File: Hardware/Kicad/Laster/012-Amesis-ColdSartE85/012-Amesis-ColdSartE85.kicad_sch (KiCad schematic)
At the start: 1 part

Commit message: kicad en cour
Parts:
- added G2/G62_InPut_IAT, G2/G62_OutPut_IAT: Conn_01x04_Male, symbol Connector:Conn_01x04_Male
- added IAT_Interne: R_Potentiometer, symbol Device:R_Potentiometer
- added Jumpers_Option: Conn_01x03_Male, symbol Connector:Conn_01x03_Male
- added X9C103S: Conn_01x08_Male, symbol Connector:Conn_01x08_Male
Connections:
- net at A?.26 (A7): now also IAT_Interne.2
- net at A?.27 (+5V): now also IAT_Interne.3
- net GND: now reaches A?.29 (GND)
- net GND: now also A?.4 (GND), IAT_Interne.1
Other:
- title: (none) -> 012-Amesis-ColdStartE85
- moved on the sheet: A?
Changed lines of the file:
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@@
   (paper "A4")
   (title_block
-    (date "2022-09-11")
-    (rev "v0.01")
-  )
-  (symbol (lib_id "MCU_Module:Arduino_Nano_v3.x") (at 129.794 87.122 0) (unit 1)
-    (in_bom yes) (on_board yes) (fields_autoplaced)
-    (property "Reference" "A?" (id 0) (at 134.3534 112.1315 0)
+    (title "012-Amesis-ColdStartE85")
+    (date "2022-09-15")
+    (rev "v0.01_Golf 1.6L 16v ")
+  )
+  (junction (at 133.858 97.282) (diameter 0) (color 0 0 0 0)
+  )
+  (junction (at 136.398 97.282) (diameter 0) (color 0 0 0 0)
+  )
+  (wire (pts (xy 168.402 83.82) (xy 168.402 39.624))
+    (stroke (width 0) (type default) (color 0 0 0 0))
+  )
+  (wire (pts (xy 136.398 97.282) (xy 133.858 97.282))
+    (stroke (width 0) (type default) (color 0 0 0 0))
+  )
+  (wire (pts (xy 168.402 97.282) (xy 136.398 97.282))
+    (stroke (width 0) (type default) (color 0 0 0 0))
+  )
+  (wire (pts (xy 168.402 39.624) (xy 138.938 39.624))
+    (stroke (width 0) (type default) (color 0 0 0 0))
+  )
+  (wire (pts (xy 133.858 97.282) (xy 133.858 95.25))
+    (stroke (width 0) (type default) (color 0 0 0 0))
+  )
+  (wire (pts (xy 146.558 87.63) (xy 164.592 87.63))
+    (stroke (width 0) (type default) (color 0 0 0 0))
+  )
+  (wire (pts (xy 133.858 98.298) (xy 133.858 97.282))
+    (stroke (width 0) (type default) (color 0 0 0 0))
+  )
+  (wire (pts (xy 168.402 91.44) (xy 168.402 97.282))
+    (stroke (width 0) (type default) (color 0 0 0 0))
+  )
+  (wire (pts (xy 138.938 39.624) (xy 138.938 44.45))
+    (stroke (width 0) (type default) (color 0 0 0 0))
+  )
+  (wire (pts (xy 136.398 95.25) (xy 136.398 97.282))
+    (stroke (width 0) (type default) (color 0 0 0 0))
+  )
+  (symbol (lib_id "power:GND") (at 128.27 23.622 0) (unit 1)
+    (in_bom yes) (on_board yes) (fields_autoplaced)
+    (property "Reference" "#PWR?" (id 0) (at 128.27 29.972 0)
+      (effects (font (size 1.27 1.27)) hide)
+    )
+    (property "Value" "GND" (id 1) (at 128.27 28.1845 0))
+    (property "Footprint" "" (id 2) (at 128.27 23.622 0)
+      (effects (font (size 1.27 1.27)) hide)
+    )
+    (property "Datasheet" "" (id 3) (at 128.27 23.622 0)
+      (effects (font (size 1.27 1.27)) hide)
+    )
+    (pin "1")
+  )
+  (symbol (lib_id "Connector:Conn_01x04_Male") (at 80.264 76.708 0) (unit 1)
+    (in_bom yes) (on_board yes)
+    (property "Reference" "G2/G62_OutPut_IAT" (id 0) (at 69.088 75.946 0))
+    (property "Value" "Conn_01x04_Male" (id 1) (at 68.834 78.486 0))
+    (property "Footprint" "" (id 2) (at 80.264 76.708 0)
+      (effects (font (size 1.27 1.27)) hide)
+    )
+    (property "Datasheet" "~" (id 3) (at 80.264 76.708 0)
+      (effects (font (size 1.27 1.27)) hide)
+    )
+    (pin "1_G2_+")
+    (pin "2_G2_-")
+    (pin "3_G62_+")
+    (pin "4_G62_-")
+  )
+  (symbol (lib_name "Conn_01x04_Male_1") (lib_id "Connector:Conn_01x04_Male") (at 80.264 53.086 0) (unit 1)
+    (in_bom yes) (on_board yes)
+    (property "Reference" "G2/G62_InPut_IAT" (id 0) (at 70.104 52.07 0))
+    (property "Value" "Conn_01x04_Male" (id 1) (at 69.85 54.356 0))
+    (property "Footprint" "" (id 2) (at 80.264 53.086 0)
+      (effects (font (size 1.27 1.27)) hide)
+    )
+    (property "Datasheet" "~" (id 3) (at 80.264 53.086 0)
+      (effects (font (size 1.27 1.27)) hide)
+    )
+    (pin "1_G2_+")
+    (pin "2_G2_-")
+    (pin "3_G62_+")
+    (pin "4_G62_-")
+  )
+  (symbol (lib_id "power:+5V") (at 122.174 26.162 0) (unit 1)
+    (in_bom yes) (on_board yes) (fields_autoplaced)
+    (property "Reference" "#PWR?" (id 0) (at 122.174 29.972 0)
+      (effects (font (size 1.27 1.27)) hide)
+    )
+    (property "Value" "+5V" (id 1) (at 122.174 22.5575 0))
+    (property "Footprint" "" (id 2) (at 122.174 26.162 0)
+      (effects (font (size 1.27 1.27)) hide)
+    )
+    (property "Datasheet" "" (id 3) (at 122.174 26.162 0)
+      (effects (font (size 1.27 1.27)) hide)
+    )
+    (pin "1")
+  )
+  (symbol (lib_id "MCU_Module:Arduino_Nano_v3.x") (at 133.858 69.85 0) (unit 1)
+    (in_bom yes) (on_board yes) (fields_autoplaced)
+    (property "Reference" "A?" (id 0) (at 138.4174 94.8595 0)
       (effects (font (size 1.27 1.27)) (justify left))
     )
-    (property "Value" "Arduino_Nano_v3.x" (id 1) (at 134.3534 114.9066 0)
+    (property "Value" "Arduino_Nano_v3.x" (id 1) (at 138.4174 97.6346 0)
       (effects (font (size 1.27 1.27)) (justify left))
     )
-    (property "Footprint" "Module:Arduino_Nano" (id 2) (at 129.794 87.122 0)
+    (property "Footprint" "Module:Arduino_Nano" (id 2) (at 133.858 69.85 0)
       (effects (font (size 1.27 1.27) italic) hide)
     )
-    (property "Datasheet" "http://www.mouser.com/pdfdocs/Gravitech_Arduino_Nano3_0.pdf" (id 3) (at 129.794 87.122 0)
+    (property "Datasheet" "http://www.mouser.com/pdfdocs/Gravitech_Arduino_Nano3_0.pdf" (id 3) (at 133.858 69.85 0)
       (effects (font (size 1.27 1.27)) hide)
     )
@@
     (pin "9")
   )
+  (symbol (lib_id "Connector:Conn_01x08_Male") (at 175.768 67.31 0) (unit 1)
+    (in_bom yes) (on_board yes)
+    (property "Reference" "X9C103S" (id 0) (at 177.8 53.594 0))
+    (property "Value" "Conn_01x08_Male" (id 1) (at 178.308 56.388 0))
+    (property "Footprint" "" (id 2) (at 175.768 67.31 0)
+      (effects (font (size 1.27 1.27)) hide)
+    )
+    (property "Datasheet" "~" (id 3) (at 175.768 67.31 0)
+      (effects (font (size 1.27 1.27)) hide)
+    )
+    (pin "1")
+    (pin "2")
+    (pin "3")
+    (pin "4")
+    (pin "5")
+    (pin "6")
+    (pin "7")
+    (pin "8")
+  )
+  (symbol (lib_id "power:GND") (at 133.858 98.298 0) (unit 1)
+    (in_bom yes) (on_board yes) (fields_autoplaced)
+    (property "Reference" "#PWR?" (id 0) (at 133.858 104.648 0)
+      (effects (font (size 1.27 1.27)) hide)
+    )
+    (property "Value" "GND" (id 1) (at 133.858 102.8605 0))
+    (property "Footprint" "" (id 2) (at 133.858 98.298 0)
+      (effects (font (size 1.27 1.27)) hide)
+    )
+    (property "Datasheet" "" (id 3) (at 133.858 98.298 0)
+      (effects (font (size 1.27 1.27)) hide)
+    )
+    (pin "1")
+  )
+  (symbol (lib_id "Connector:Conn_01x03_Male") (at 94.488 93.472 0) (unit 1)
+    (in_bom yes) (on_board yes)
+    (property "Reference" "Jumpers_Option" (id 0) (at 85.344 90.932 0))
+    (property "Value" "Conn_01x03_Male" (id 1) (at 84.582 93.98 0))
+    (property "Footprint" "" (id 2) (at 94.488 93.472 0)
+      (effects (font (size 1.27 1.27)) hide)
+    )
+    (property "Datasheet" "~" (id 3) (at 94.488 93.472 0)
+      (effects (font (size 1.27 1.27)) hide)
+    )
+    (pin "1")
+    (pin "2")
+    (pin "3")
+  )
+  (symbol (lib_id "Device:R_Potentiometer") (at 168.402 87.63 180) (unit 1)
+    (in_bom yes) (on_board yes) (fields_autoplaced)
+    (property "Reference" "IAT_Interne" (id 0) (at 170.18 86.7215 0)
+      (effects (font (size 1.27 1.27)) (justify right))
+    )
+    (property "Value" "R_Potentiometer" (id 1) (at 170.18 89.4966 0)
+      (effects (font (size 1.27 1.27)) (justify right))
+    )
+    (property "Footprint" "" (id 2) (at 168.402 87.63 0)
+      (effects (font (size 1.27 1.27)) hide)
+    )
+    (property "Datasheet" "~" (id 3) (at 168.402 87.63 0)
+      (effects (font (size 1.27 1.27)) hide)
+    )
+    (pin "1")
+    (pin "2")
+    (pin "3")
+  )
+  (symbol (lib_id "power:+12V") (at 116.84 25.654 0) (unit 1)
+    (in_bom yes) (on_board yes) (fields_autoplaced)
+    (property "Reference" "#PWR?" (id 0) (at 116.84 29.464 0)
+      (effects (font (size 1.27 1.27)) hide)
+    )
+    (property "Value" "+12V" (id 1) (at 116.84 22.0495 0))
+    (property "Footprint" "" (id 2) (at 116.84 25.654 0)
+      (effects (font (size 1.27 1.27)) hide)
+    )
+    (property "Datasheet" "" (id 3) (at 116.84 25.654 0)
+      (effects (font (size 1.27 1.27)) hide)
+    )
+    (pin "1")
+  )
   (sheet_instances
     (path "/" (page "1"))
   )
   (symbol_instances
+    (path "/11b83b14-b3d5-4a5f-b040-8b64c55872d9"
+      (reference "#PWR?") (unit 1) (value "GND") (footprint "")
+    )
+    (path "/66566cdb-d9d4-4c3f-b252-46e4ed2ba901"
+      (reference "#PWR?") (unit 1) (value "+5V") (footprint "")
+    )
+    (path "/c585af0b-16a9-4b91-b036-95392fa023ef"
+      (reference "#PWR?") (unit 1) (value "GND") (footprint "")
+    )
+    (path "/f5806723-7567-4637-88f6-9c629f0e4fe1"
+      (reference "#PWR?") (unit 1) (value "+12V") (footprint "")
+    )
     (path "/6832f754-a6e6-478a-bd86-858502b6adf6"
       (reference "A?") (unit 1) (value "Arduino_Nano_v3.x") (footprint "Module:Arduino_Nano")
     )
-  )
+    (path "/58fa8ecc-baf9-437b-a607-8a18b6973e48"
+      (reference "G2/G62_InPut_IAT") (unit 1) (value "Conn_01x04_Male") (footprint "")
+    )
+    (path "/3f3de678-126f-48f3-83bd-3e97741caa7c"
+      (reference "G2/G62_OutPut_IAT") (unit 1) (value "Conn_01x04_Male") (footprint "")
+    )
+    (path "/efe8e9bc-5367-4c16-bae5-490a0bb31048"
+      (reference "IAT_Interne") (unit 1) (value "R_Potentiometer") (footprint "")
+    )
+    (path "/dd244b1d-d433-47da-8791-7b2844dc0094"
+      (reference "Jumpers_Option") (unit 1) (value "Conn_01x03_Male") (footprint "")
+    )
+    (path "/78330401-ec21-4893-9361-e449b5c6c1e8"
+      (reference "X9C103S") (unit 1) (value "Conn_01x08_Male") (footprint "")
+    )
+  )

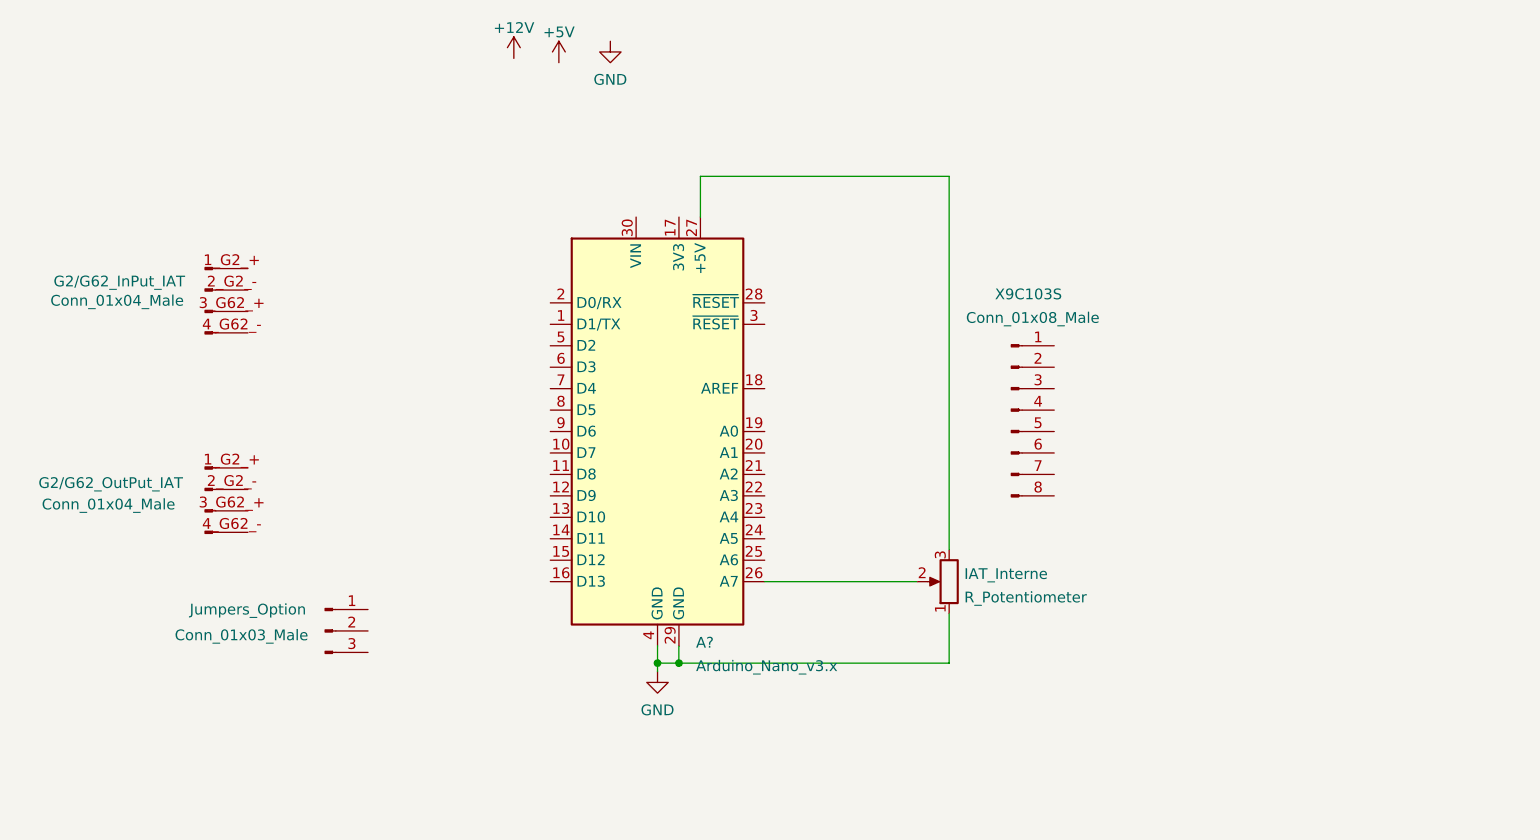
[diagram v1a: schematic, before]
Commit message: Création du PCB
En cour. le controleur de rootage affiche quelques erreurs
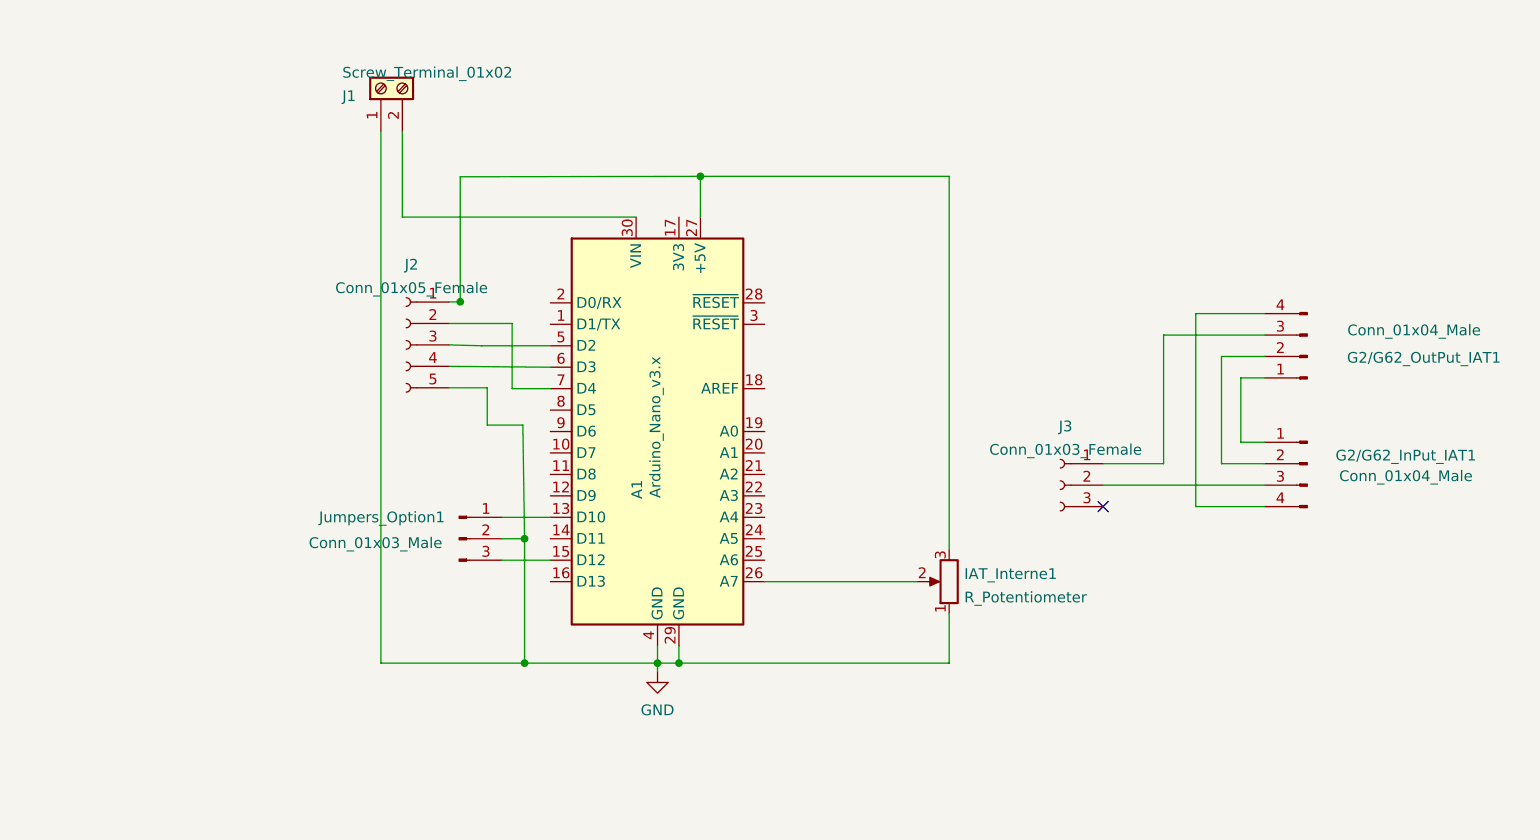
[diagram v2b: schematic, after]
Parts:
- removed X9C103S: Conn_01x08_Male, symbol Connector:Conn_01x08_Male
- added J1: Screw_Terminal_01x02, TerminalBlock:TerminalBlock_bornier-2_P5.08mm, symbol Connector:Screw_Terminal_01x02
- added J2: Conn_01x05_Female, Connector_PinSocket_2.54mm:PinSocket_1x05_P2.54mm_Vertical, symbol Connector:Conn_01x05_Female
- added J3: Conn_01x03_Female, Connector_PinSocket_2.54mm:PinSocket_1x03_P2.54mm_Vertical, symbol Connector:Conn_01x03_Female
- G2/G62_InPut_IAT1: renamed from G2/G62_InPut_IAT; footprint (none) -> TerminalBlock:TerminalBlock_bornier-4_P5.08mm
- G2/G62_OutPut_IAT1: renamed from G2/G62_OutPut_IAT; footprint (none) -> TerminalBlock:TerminalBlock_bornier-4_P5.08mm
- IAT_Interne1: renamed from IAT_Interne; footprint (none) -> Connector_PinSocket_2.54mm:PinSocket_1x03_P2.54mm_Vertical
- Jumpers_Option1: renamed from Jumpers_Option; footprint (none) -> Connector_PinHeader_2.54mm:PinHeader_1x03_P2.54mm_Vertical
- gave numbers to parts that had none: 1
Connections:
- net GND: now also Jumpers_Option1.2 (Pin_2), J1.1 (Pin_1), J2.5 (Pin_5)
- net at A1.13 (D10): now also Jumpers_Option1.1 (Pin_1)
- net at A1.15 (D12): now also Jumpers_Option1.3 (Pin_3)
- net at A1.27 (+5V), IAT_Interne1.3: now also J2.1 (Pin_1)
- net at A1.30 (VIN): now also J1.2 (Pin_2)
- net at A1.5 (D2): now also J2.3 (Pin_3)
- net at A1.6 (D3): now also J2.4 (Pin_4)
- net at A1.7 (D4): now also J2.2 (Pin_2)
- new net: G2/G62_InPut_IAT1.1 (Pin_1), G2/G62_OutPut_IAT1.1 (Pin_1)
- new net: G2/G62_InPut_IAT1.2 (Pin_2), G2/G62_OutPut_IAT1.2 (Pin_2)
- new net: G2/G62_OutPut_IAT1.3 (Pin_3), J3.1 (Pin_1)
- new net: G2/G62_InPut_IAT1.4 (Pin_4), G2/G62_OutPut_IAT1.4 (Pin_4)
- new net: G2/G62_InPut_IAT1.3 (Pin_3), J3.2 (Pin_2)
- no-connect marks 0 -> 1
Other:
- moved on the sheet: G2/G62_InPut_IAT1, G2/G62_OutPut_IAT1, Jumpers_Option1

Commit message: maj
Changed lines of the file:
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@@
       (effects (font (size 1.27 1.27)) hide)
     )
+    (pin "1")
     (pin "2")
-    (pin "1")
   )
   (symbol (lib_name "Conn_01x03_Female_1") (lib_id "Connector:Conn_01x03_Female") (at 181.5592 76.2 0) (mirror y) (unit 1)
-    (in_bom yes) (on_board yes) (fields_autoplaced)
-    (property "Reference" "J3" (id 0) (at 182.1942 69.2363 0))
-    (property "Value" "Conn_01x03_Female" (id 1) (at 182.1942 72.0114 0))
+    (in_bom yes) (on_board yes)
+    (property "Reference" "J3" (id 0) (at 178.308 62.23 0))
+    (property "Value" "Conn_01x03_Female" (id 1) (at 178.308 66.548 0))
     (property "Footprint" "Connector_PinSocket_2.54mm:PinSocket_1x03_P2.54mm_Vertical" (id 2) (at 181.5592 76.2 0)
       (effects (font (size 1.27 1.27)) hide)
